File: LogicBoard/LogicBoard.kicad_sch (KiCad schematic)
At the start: 0 parts

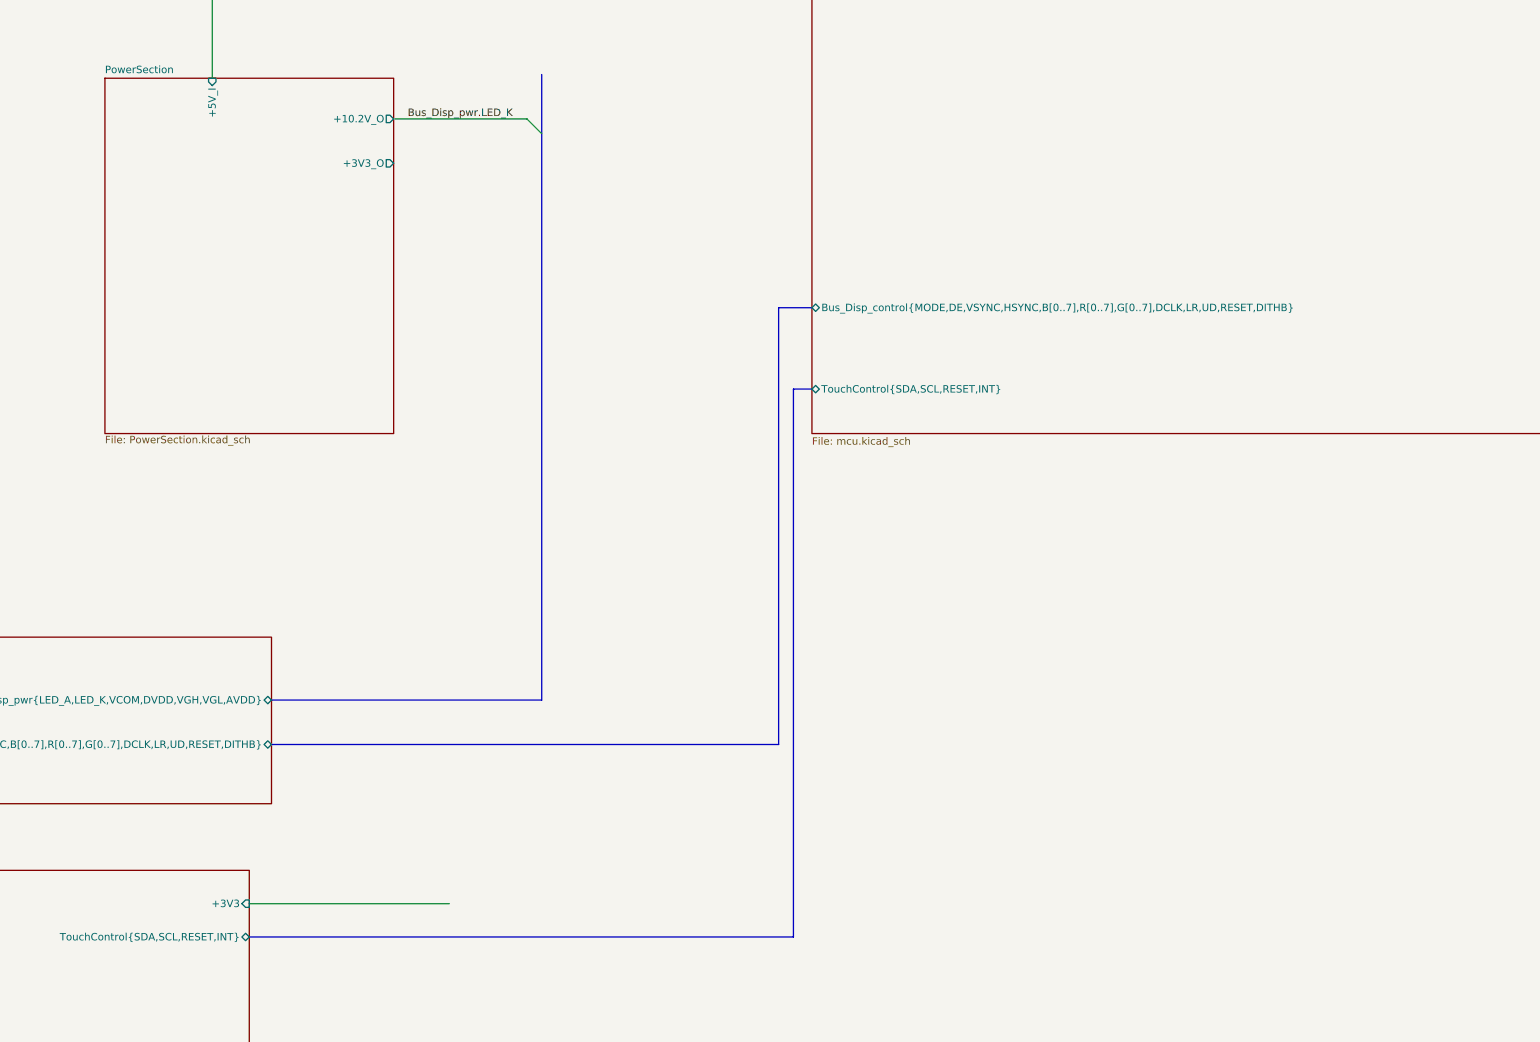
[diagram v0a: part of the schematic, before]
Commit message: added jlcpcb nums to some parts
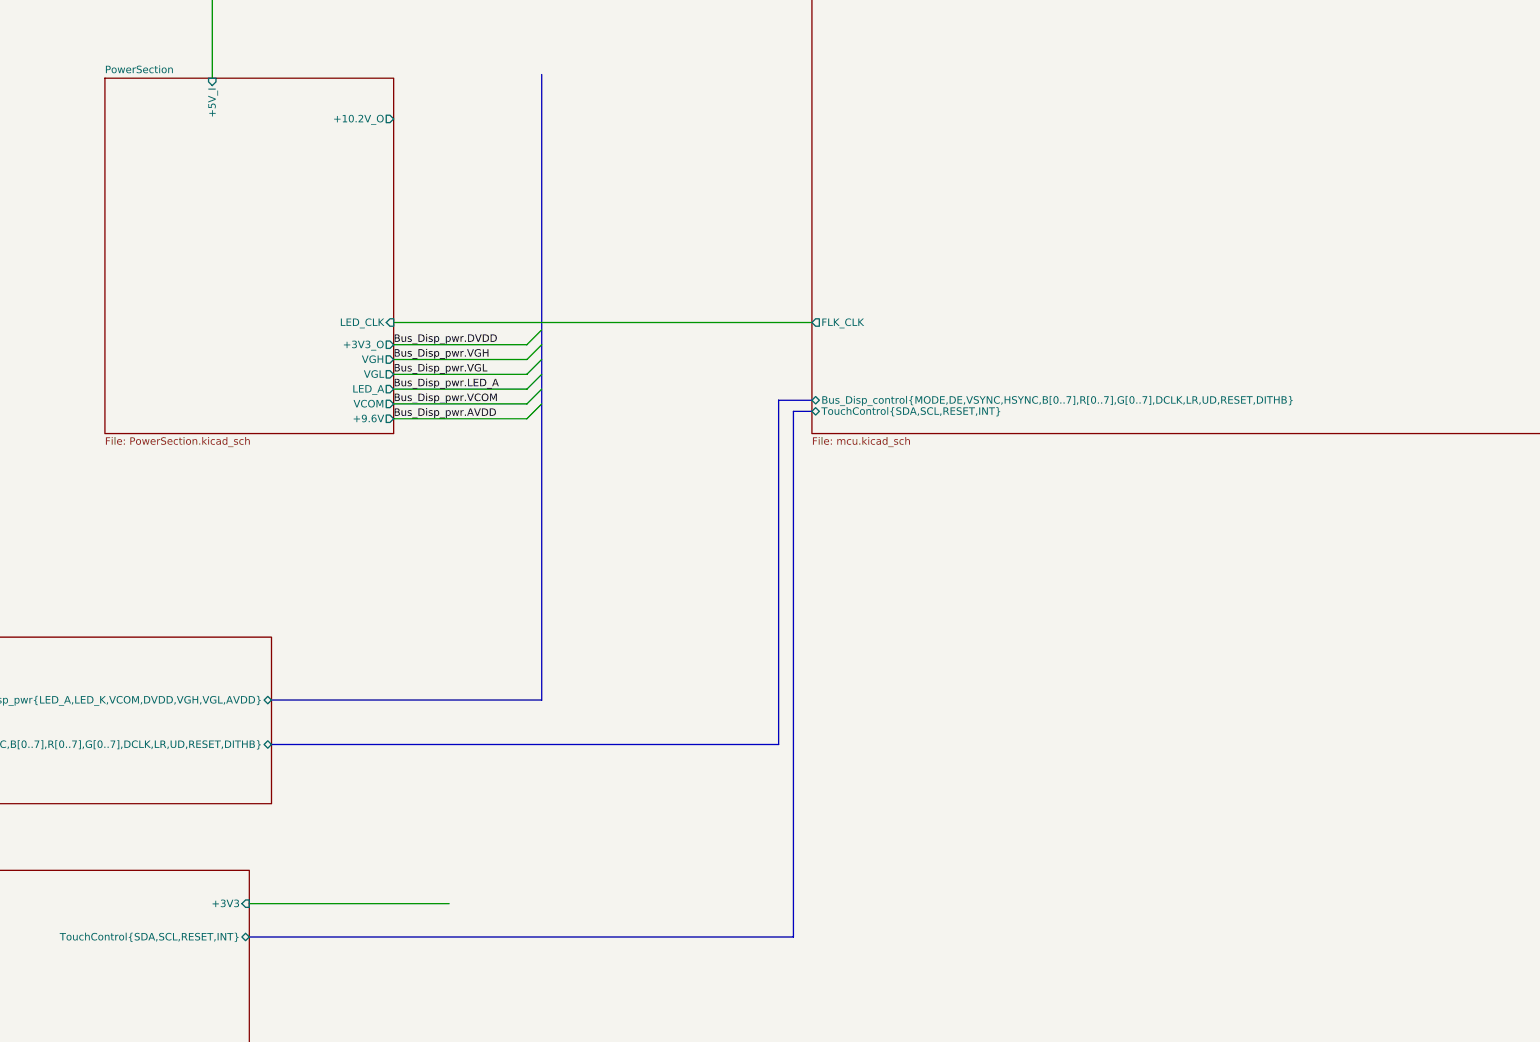
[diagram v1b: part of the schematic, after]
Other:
- sheet PowerSection ports: added +9.6V, LED_A, LED_CLK, VCOM, VGH, VGL; removed none
- sheet mcu ports: added FLK_CLK; removed none
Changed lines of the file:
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@@
 	(paper "A2")
 	(bus_entry
-		(at 201.295 158.75)
-		(size -2.54 -2.54)
+		(at 201.295 202.565)
+		(size -2.54 2.54)
+		(stroke
+			(width 0)
+			(type default)
+		)
+	)
+	(bus_entry
+		(at 201.295 200.025)
+		(size -2.54 2.54)
+		(stroke
+			(width 0)
+			(type default)
+		)
+	)
+	(bus_entry
+		(at 201.295 194.945)
+		(size -2.54 2.54)
+		(stroke
+			(width 0)
+			(type default)
+		)
+	)
+	(bus_entry
+		(at 201.295 192.405)
+		(size -2.54 2.54)
+		(stroke
+			(width 0)
+			(type default)
+		)
+	)
+	(bus_entry
+		(at 201.295 205.105)
+		(size -2.54 2.54)
+		(stroke
+			(width 0)
+			(type default)
+		)
+	)
+	(bus_entry
+		(at 201.295 197.485)
+		(size -2.54 2.54)
+		(stroke
+			(width 0)
+			(type default)
+		)
+	)
+	(wire
+		(pts
+			(xy 198.755 197.485) (xy 175.895 197.485)
+		)
+		(stroke
+			(width 0)
+			(type default)
+		)
+	)
+	(wire
+		(pts
+			(xy 175.895 191.135) (xy 247.65 191.135)
+		)
+		(stroke
+			(width 0)
+			(type default)
+		)
+	)
+	(wire
+		(pts
+			(xy 198.755 207.645) (xy 175.895 207.645)
+		)
+		(stroke
+			(width 0)
+			(type default)
+		)
+	)
+	(bus
+		(pts
+			(xy 244.475 296.545) (xy 244.475 206.375)
+		)
+		(stroke
+			(width 0)
+			(type default)
+		)
+	)
+	(bus
+		(pts
+			(xy 154.94 263.525) (xy 241.935 263.525)
+		)
 		(stroke
 			(width 0)
@@
 		)
 	)
-	(bus
-		(pts
-			(xy 244.475 296.545) (xy 244.475 202.565)
-		)
-		(stroke
-			(width 0)
-			(type default)
-		)
-	)
-	(bus
-		(pts
-			(xy 154.94 263.525) (xy 241.935 263.525)
-		)
-		(stroke
-			(width 0)
-			(type default)
-		)
-	)
 	(wire
 		(pts
@@
 	(wire
 		(pts
-			(xy 176.149 156.21) (xy 198.755 156.21)
-		)
-		(stroke
-			(width 0)
-			(type default)
-		)
-	)
-	(wire
-		(pts
 			(xy 172.72 104.775) (xy 247.65 104.775)
 		)
@@
 		)
 	)
+	(wire
+		(pts
+			(xy 175.895 200.025) (xy 198.755 200.025)
+		)
+		(stroke
+			(width 0)
+			(type default)
+		)
+	)
 	(bus
 		(pts
@@
 	(bus
 		(pts
-			(xy 241.935 263.525) (xy 241.935 188.595)
+			(xy 241.935 263.525) (xy 241.935 204.47)
 		)
 		(stroke
@@
 	(bus
 		(pts
-			(xy 244.475 202.565) (xy 247.65 202.565)
+			(xy 244.475 206.375) (xy 247.65 206.375)
+		)
+		(stroke
+			(width 0)
+			(type default)
+		)
+	)
+	(wire
+		(pts
+			(xy 198.755 205.105) (xy 175.895 205.105)
 		)
 		(stroke
@@
 		)
 	)
+	(wire
+		(pts
+			(xy 198.755 202.565) (xy 175.895 202.565)
+		)
+		(stroke
+			(width 0)
+			(type default)
+		)
+	)
+	(wire
+		(pts
+			(xy 198.755 194.945) (xy 175.895 194.945)
+		)
+		(stroke
+			(width 0)
+			(type default)
+		)
+	)
 	(bus
 		(pts
@@
 	(bus
 		(pts
-			(xy 241.935 188.595) (xy 247.65 188.595)
+			(xy 241.935 204.47) (xy 247.65 204.47)
 		)
 		(stroke
@@
 		)
 	)
-	(label "Bus_Disp_pwr.LED_K"
-		(at 178.308 156.21 0)
+	(label "Bus_Disp_pwr.VCOM"
+		(at 175.895 205.105 0)
+		(effects
+			(font
+				(size 1.27 1.27)
+			)
+			(justify left bottom)
+		)
+	)
+	(label "Bus_Disp_pwr.LED_A"
+		(at 175.895 202.565 0)
+		(effects
+			(font
+				(size 1.27 1.27)
+			)
+			(justify left bottom)
+		)
+	)
+	(label "Bus_Disp_pwr.VGL"
+		(at 175.895 200.025 0)
+		(effects
+			(font
+				(size 1.27 1.27)
+			)
+			(justify left bottom)
+		)
+	)
+	(label "Bus_Disp_pwr.VGH"
+		(at 175.895 197.485 0)
+		(effects
+			(font
+				(size 1.27 1.27)
+			)
+			(justify left bottom)
+		)
+	)
+	(label "Bus_Disp_pwr.DVDD"
+		(at 175.895 194.945 0)
+		(effects
+			(font
+				(size 1.27 1.27)
+			)
+			(justify left bottom)
+		)
+	)
+	(label "Bus_Disp_pwr.AVDD"
+		(at 175.895 207.645 0)
 		(effects
 			(font
@@
 		)
 		(property "Sheetfile" "PowerSection.kicad_sch"
-			(at 126.365 210.5156 0)
+			(at 126.365 210.7696 0)
 			(show_name no)
 			(do_not_autoplace no)
@@
 		)
 		(pin "+3V3_O" output
-			(at 175.895 163.83 0)
+			(at 175.895 194.945 0)
 			(effects
 				(font
@@
 		(pin "+10.2V_O" output
 			(at 175.895 156.21 0)
+			(effects
+				(font
+					(size 1.27 1.27)
+				)
+				(justify right)
+			)
+		)
+		(pin "VGL" output
+			(at 175.895 200.025 0)
+			(effects
+				(font
+					(size 1.27 1.27)
+				)
+				(justify right)
+			)
+		)
+		(pin "LED_A" output
+			(at 175.895 202.565 0)
+			(effects
+				(font
+					(size 1.27 1.27)
+				)
+				(justify right)
+			)
+		)
+		(pin "VCOM" output
+			(at 175.895 205.105 0)
+			(effects
+				(font
+					(size 1.27 1.27)
+				)
+				(justify right)
+			)
+		)
+		(pin "VGH" output
+			(at 175.895 197.485 0)
+			(effects
+				(font
+					(size 1.27 1.27)
+				)
+				(justify right)
+			)
+		)
+		(pin "+9.6V" output
+			(at 175.895 207.645 0)
+			(effects
+				(font
+					(size 1.27 1.27)
+				)
+				(justify right)
+			)
+		)
+		(pin "LED_CLK" input
+			(at 175.895 191.135 0)
 			(effects
 				(font
@@
 		(pin "Bus_Disp_control{MODE,DE,VSYNC,HSYNC,B[0..7],R[0..7],G[0..7],DCLK,LR,UD,RESET,DITHB}"
 			bidirectional
-			(at 247.65 188.595 180
+			(at 247.65 204.47 180
 			)
 			(effects
@@
 		)
 		(pin "TouchControl{SDA,SCL,RESET,INT}" bidirectional
-			(at 247.65 202.565 180)
+			(at 247.65 206.375 180)
 			(effects
 				(font
@@
 			(effects
 				(font
+					(size 1.27 1.27)
+				)
+				(justify left)
+			)
+		)
+		(pin "FLK_CLK" output
+			(at 247.65 191.135 180)
+			(effects
+				(font
